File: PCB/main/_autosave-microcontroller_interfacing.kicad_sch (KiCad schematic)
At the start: 19 parts, among them U3 CH340G, U4 USB_Micro_B, U5 AT24C256C-SSHL-T, X1 12MHz Crystal

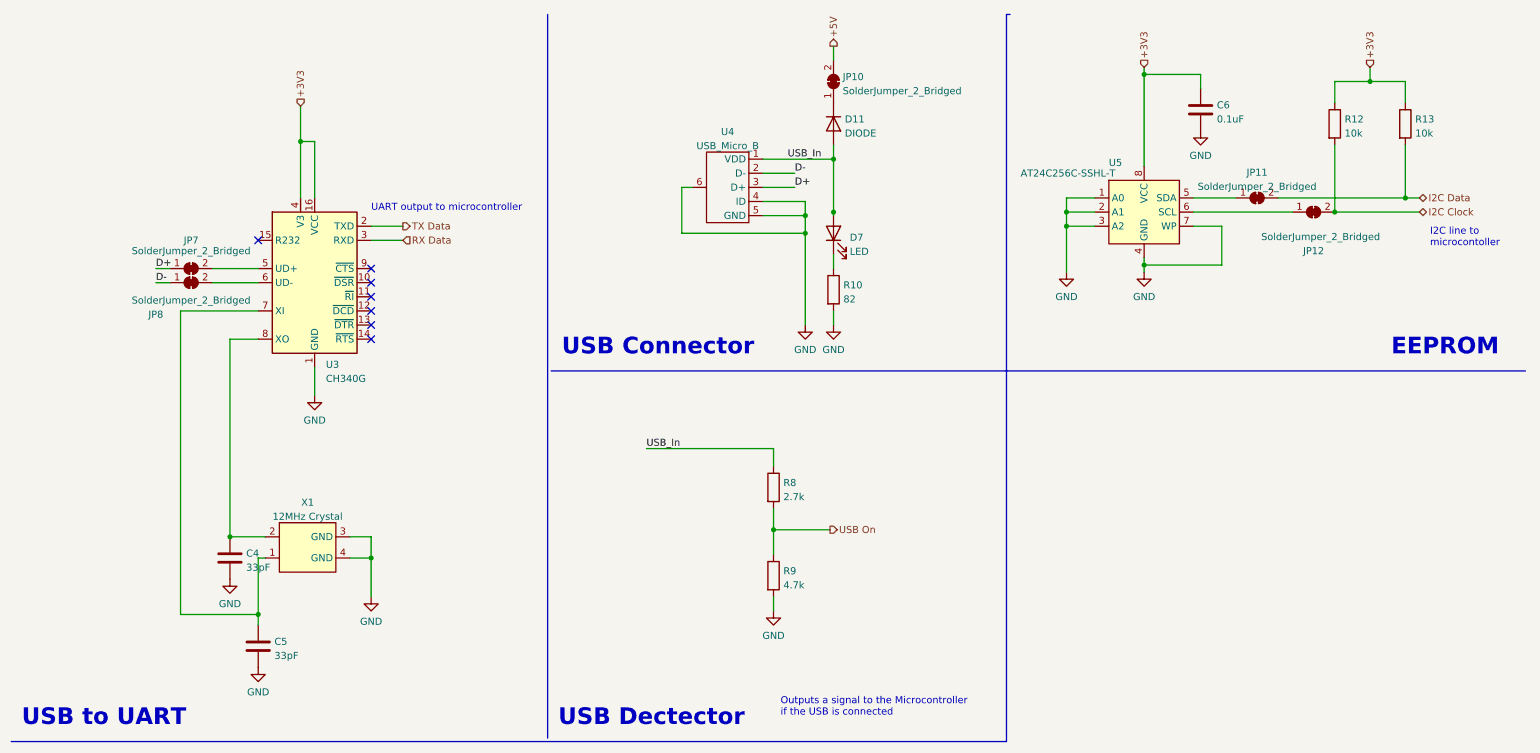
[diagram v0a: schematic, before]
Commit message: Add power flags
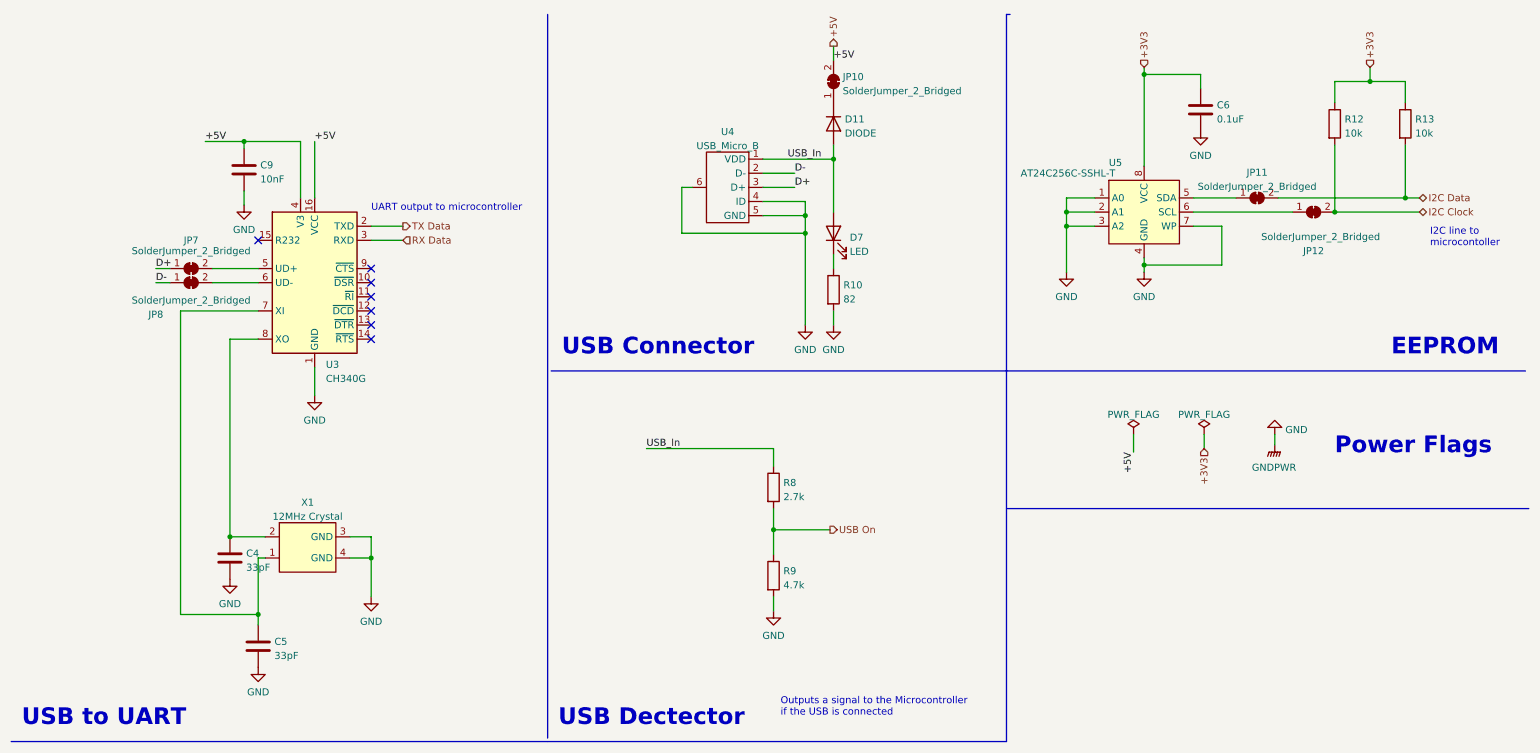
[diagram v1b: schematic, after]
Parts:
- added C9: 10nF, Capacitor_SMD:C_0402_1005Metric, symbol Device:C
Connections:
- net +3V3: no longer U3.16 (VCC), U3.4 (V3)
- net +5V: now also U3.16 (VCC), U3.4 (V3), C9.1
- net GND: now also C9.2
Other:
- note added: "Power Flags"
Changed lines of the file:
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@@
   (junction (at 160.02 38.1) (diameter 0) (color 0 0 0 0)
   )
-  (junction (at 160.02 47.625) (diameter 0) (color 0 0 0 0)
-  )
   (junction (at 201.93 50.165) (diameter 0) (color 0 0 0 0)
   )
@@
   (junction (at 154.94 51.435) (diameter 0) (color 0 0 0 0)
   )
-  (junction (at 64.135 34.925) (diameter 0) (color 0 0 0 0)
+  (junction (at 53.975 34.925) (diameter 0) (color 0 0 0 0)
   )
   (junction (at 215.9 57.15) (diameter 0) (color 0 0 0 0)
@@
     (stroke (width 0) (type default) (color 0 0 0 0))
   )
+  (wire (pts (xy 53.975 34.925) (xy 64.135 34.925))
+    (stroke (width 0) (type default) (color 0 0 0 0))
+  )
   (wire (pts (xy 66.675 75.565) (xy 66.675 80.645))
     (stroke (width 0) (type default) (color 0 0 0 0))
@@
     (stroke (width 0) (type default) (color 0 0 0 0))
   )
-  (wire (pts (xy 64.135 28.575) (xy 64.135 34.925))
+  (wire (pts (xy 46.99 34.925) (xy 53.975 34.925))
     (stroke (width 0) (type default) (color 0 0 0 0))
   )
@@
     (stroke (width 0) (type default) (color 0 0 0 0))
   )
-  (wire (pts (xy 160.02 47.625) (xy 160.02 48.26))
-    (stroke (width 0) (type default) (color 0 0 0 0))
-  )
   (wire (pts (xy 201.93 50.165) (xy 201.93 58.42))
     (stroke (width 0) (type default) (color 0 0 0 0))
@@
     (stroke (width 0) (type default) (color 0 0 0 0))
   )
+  (wire (pts (xy 53.975 34.925) (xy 53.975 36.195))
+    (stroke (width 0) (type default) (color 0 0 0 0))
+  )
   (wire (pts (xy 51.435 70.485) (xy 56.515 70.485))
     (stroke (width 0) (type default) (color 0 0 0 0))
@@
     (stroke (width 0) (type default) (color 0 0 0 0))
   )
+  (wire (pts (xy 226.695 87.63) (xy 226.695 90.17))
+    (stroke (width 0) (type default) (color 0 0 0 0))
+  )
   (wire (pts (xy 56.515 109.855) (xy 56.515 120.015))
     (stroke (width 0) (type default) (color 0 0 0 0))
@@
     (stroke (width 0) (type default) (color 0 0 0 0))
   )
+  (polyline (pts (xy 191.135 100.965) (xy 285.115 100.965))
+    (stroke (width 0) (type default) (color 0 0 0 0))
+  )
   (wire (pts (xy 160.02 55.245) (xy 160.02 57.785))
     (stroke (width 0) (type default) (color 0 0 0 0))
@@
     (stroke (width 0) (type default) (color 0 0 0 0))
   )
+  (wire (pts (xy 213.995 87.63) (xy 213.995 90.805))
+    (stroke (width 0) (type default) (color 0 0 0 0))
+  )
   (wire (pts (xy 160.02 65.405) (xy 160.02 67.945))
     (stroke (width 0) (type default) (color 0 0 0 0))
@@
     (stroke (width 0) (type default) (color 0 0 0 0))
   )
-  (wire (pts (xy 64.135 34.925) (xy 66.675 34.925))
-    (stroke (width 0) (type default) (color 0 0 0 0))
-  )
   (wire (pts (xy 42.545 65.405) (xy 56.515 65.405))
     (stroke (width 0) (type default) (color 0 0 0 0))
@@
   )
   (wire (pts (xy 154.94 51.435) (xy 154.94 67.945))
+    (stroke (width 0) (type default) (color 0 0 0 0))
+  )
+  (wire (pts (xy 53.975 43.815) (xy 53.975 46.355))
+    (stroke (width 0) (type default) (color 0 0 0 0))
+  )
+  (wire (pts (xy 239.395 87.63) (xy 239.395 89.535))
     (stroke (width 0) (type default) (color 0 0 0 0))
   )
@@
     (effects (font (size 1.27 1.27)) (justify left bottom))
   )
+  (text "Power Flags" (at 250.19 91.44 0)
+    (effects (font (size 3 3) (thickness 0.8) bold) (justify left bottom))
+  )
   (text "I2C line to \nmicrocontoller" (at 267.335 53.975 0)
     (effects (font (size 1.27 1.27)) (justify left bottom))
@@
     (effects (font (size 1.27 1.27)) (justify left bottom))
   )
+  (label "+5V" (at 66.675 34.925 0)
+    (effects (font (size 1.27 1.27)) (justify left bottom))
+  )
   (label "D-" (at 153.035 40.64 0)
     (effects (font (size 1.27 1.27)) (justify left bottom))
@@
     (effects (font (size 1.27 1.27)) (justify left bottom))
   )
+  (label "+5V" (at 160.02 20.32 0)
+    (effects (font (size 1.27 1.27)) (justify left bottom))
+  )
+  (label "+5V" (at 46.99 34.925 0)
+    (effects (font (size 1.27 1.27)) (justify left bottom))
+  )
   (label "D+" (at 38.1 57.785 0)
     (effects (font (size 1.27 1.27)) (justify left bottom))
+  )
+  (label "+5V" (at 213.995 90.805 270)
+    (effects (font (size 1.27 1.27)) (justify right bottom))
   )
   (label "USB_In" (at 151.765 38.1 0)
@@
     (effects (font (size 1.27 1.27)) (justify left))
   )
-  (hierarchical_label "+3V3" (shape input) (at 64.135 28.575 90)
-    (effects (font (size 1.27 1.27)) (justify left))
-  )
   (hierarchical_label "+3V3" (shape input) (at 215.9 21.59 90)
     (effects (font (size 1.27 1.27)) (justify left))
@@
   (hierarchical_label "TX Data" (shape output) (at 82.55 50.165 0)
     (effects (font (size 1.27 1.27)) (justify left))
+  )
+  (hierarchical_label "+3V3" (shape input) (at 226.695 90.17 270)
+    (effects (font (size 1.27 1.27)) (justify right))
   )
   (symbol (lib_id "power:GND") (at 215.9 58.42 0) (unit 1)
@@
     (pin "5")
     (pin "6")
+  )
+  (symbol (lib_id "power:PWR_FLAG") (at 213.995 87.63 0) (unit 1)
+    (in_bom yes) (on_board yes) (fields_autoplaced)
+    (property "Reference" "#FLG01" (id 0) (at 213.995 85.725 0)
+      (effects (font (size 1.27 1.27)) hide)
+    )
+    (property "Value" "PWR_FLAG" (id 1) (at 213.995 84.0542 0))
+    (property "Footprint" "" (id 2) (at 213.995 87.63 0)
+      (effects (font (size 1.27 1.27)) hide)
+    )
+    (property "Datasheet" "~" (id 3) (at 213.995 87.63 0)
+      (effects (font (size 1.27 1.27)) hide)
+    )
+    (pin "1")
   )
   (symbol (lib_id "Device:C") (at 226.06 29.21 0) (unit 1)
@@
     (pin "1")
   )
+  (symbol (lib_id "Device:C") (at 53.975 40.005 0) (unit 1)
+    (in_bom yes) (on_board yes) (fields_autoplaced)
+    (property "Reference" "C9" (id 0) (at 56.896 39.1703 0)
+      (effects (font (size 1.27 1.27)) (justify left))
+    )
+    (property "Value" "10nF" (id 1) (at 56.896 41.7072 0)
+      (effects (font (size 1.27 1.27)) (justify left))
+    )
+    (property "Footprint" "Capacitor_SMD:C_0402_1005Metric" (id 2) (at 54.9402 43.815 0)
+      (effects (font (size 1.27 1.27)) hide)
+    )
+    (property "Datasheet" "~" (id 3) (at 53.975 40.005 0)
+      (effects (font (size 1.27 1.27)) hide)
+    )
+    (property "JLC Part #" "C1525" (id 4) (at 53.975 40.005 0)
+      (effects (font (size 1.27 1.27)) hide)
+    )
+    (property "Price" "$0.0011" (id 5) (at 53.975 40.005 0)
+      (effects (font (size 1.27 1.27)) hide)
+    )
+    (property "Extended/Basic" "B" (id 6) (at 53.975 40.005 0)
+      (effects (font (size 1.27 1.27)) hide)
+    )
+    (pin "1")
+    (pin "2")
+  )
   (symbol (lib_id "power:GND") (at 66.675 80.645 0) (unit 1)
     (in_bom yes) (on_board yes) (fields_autoplaced)
@@
     (pin "2")
   )
+  (symbol (lib_id "power:GNDPWR") (at 239.395 89.535 0) (unit 1)
+    (in_bom yes) (on_board yes) (fields_autoplaced)
+    (property "Reference" "#PWR08" (id 0) (at 239.395 94.615 0)
+      (effects (font (size 1.27 1.27)) hide)
+    )
+    (property "Value" "GNDPWR" (id 1) (at 239.268 93.572 0))
+    (property "Footprint" "" (id 2) (at 239.395 90.805 0)
+      (effects (font (size 1.27 1.27)) hide)
+    )
+    (property "Datasheet" "" (id 3) (at 239.395 90.805 0)
+      (effects (font (size 1.27 1.27)) hide)
+    )
+    (pin "1")
+  )
   (symbol (lib_id "power:GND") (at 154.94 67.945 0) (unit 1)
     (in_bom yes) (on_board yes) (fields_autoplaced)
@@
     (pin "2")
   )
+  (symbol (lib_id "power:GND") (at 53.975 46.355 0) (unit 1)
+    (in_bom yes) (on_board yes) (fields_autoplaced)
+    (property "Reference" "#PWR02" (id 0) (at 53.975 52.705 0)
+      (effects (font (size 1.27 1.27)) hide)
+    )
+    (property "Value" "GND" (id 1) (at 53.975 50.7984 0))
+    (property "Footprint" "" (id 2) (at 53.975 46.355 0)
+      (effects (font (size 1.27 1.27)) hide)
+    )
+    (property "Datasheet" "" (id 3) (at 53.975 46.355 0)
+      (effects (font (size 1.27 1.27)) hide)
+    )
+    (pin "1")
+  )
+  (symbol (lib_id "power:GND") (at 239.395 87.63 180) (unit 1)
+    (in_bom yes) (on_board yes) (fields_autoplaced)
+    (property "Reference" "#PWR04" (id 0) (at 239.395 81.28 0)
+      (effects (font (size 1.27 1.27)) hide)
+    )
+    (property "Value" "GND" (id 1) (at 241.3 86.7938 0)
+      (effects (font (size 1.27 1.27)) (justify right))
+    )
+    (property "Footprint" "" (id 2) (at 239.395 87.63 0)
+      (effects (font (size 1.27 1.27)) hide)
+    )
+    (property "Datasheet" "" (id 3) (at 239.395 87.63 0)
+      (effects (font (size 1.27 1.27)) hide)
+    )
+    (pin "1")
+  )
+  (symbol (lib_id "power:PWR_FLAG") (at 226.695 87.63 0) (unit 1)
+    (in_bom yes) (on_board yes) (fields_autoplaced)
+    (property "Reference" "#FLG02" (id 0) (at 226.695 85.725 0)
+      (effects (font (size 1.27 1.27)) hide)
+    )
+    (property "Value" "PWR_FLAG" (id 1) (at 226.695 84.0542 0))
+    (property "Footprint" "" (id 2) (at 226.695 87.63 0)
+      (effects (font (size 1.27 1.27)) hide)
+    )
+    (property "Datasheet" "~" (id 3) (at 226.695 87.63 0)
+      (effects (font (size 1.27 1.27)) hide)
+    )
+    (pin "1")
+  )
   (symbol (lib_id "power:GND") (at 51.435 113.665 0) (unit 1)
